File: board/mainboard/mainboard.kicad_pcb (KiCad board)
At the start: 2 copper layers, 148.1 x 58.4 mm, 97 parts, among them J1 BACKL, P1 I2C, P10 BUMPERS, P12 POWER, P2 Motor1, P3 Motor2, P4 SPI, P5 DAC, P6 LINE SENSORS, P7 ANALOG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

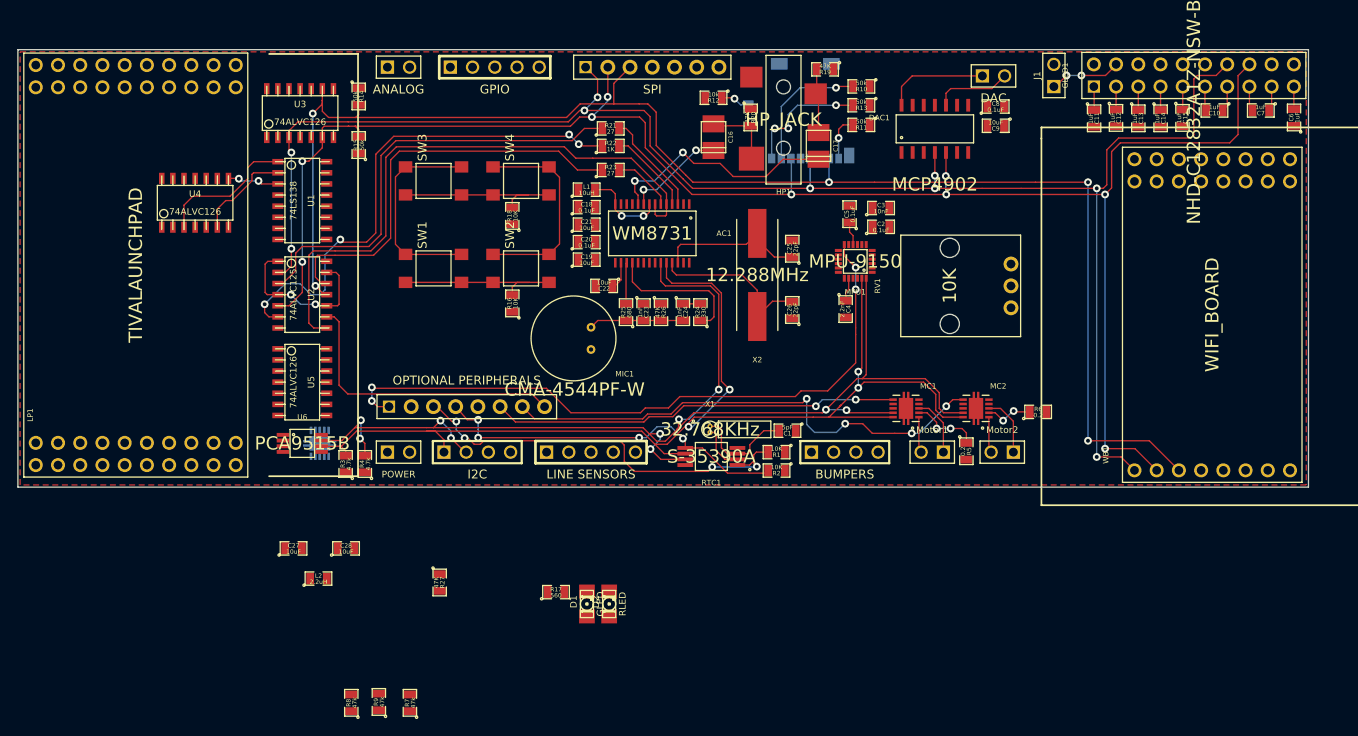
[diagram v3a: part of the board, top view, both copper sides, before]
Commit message: All but Spi_CS and power are routed.
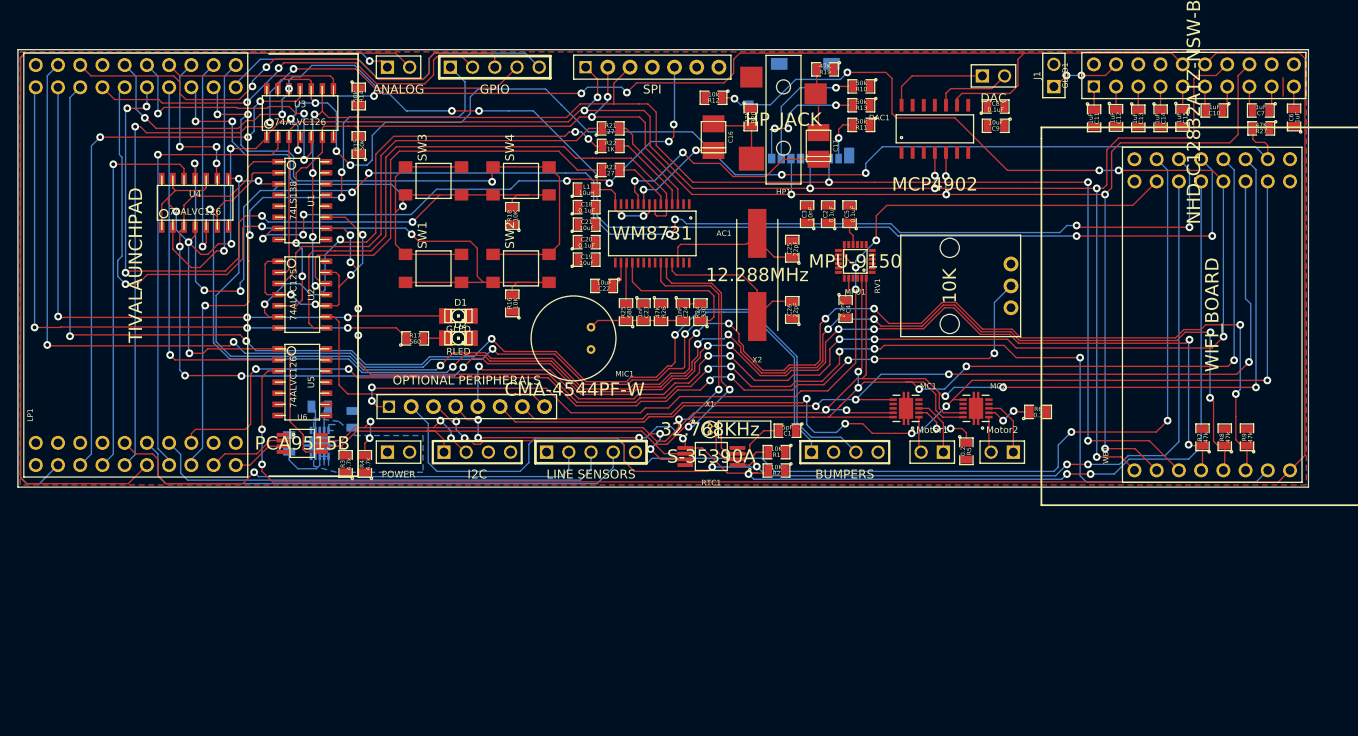
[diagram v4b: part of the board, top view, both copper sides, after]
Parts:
- C27, C28, L2: moved to B.Cu
- moved R27 107.3 mm to (269.6, 119.0), turned to 180 degrees
- moved R8 104.3 mm to (265.4, 154.3)
- moved R9 103.7 mm to (268.0, 154.3)
- moved R7 95.5 mm to (262.9, 154.3)
- moved D1 36.1 mm to (177.8, 140.4), turned to 0 degrees
- moved D2 34.9 mm to (177.8, 143.0), turned to 0 degrees
- moved R17 33.2 mm to (172.9, 143.0)
- moved L2 19.7 mm to (162.0, 150.8), turned to 180 degrees
- moved C28 14.8 mm to (165.8, 152.2), turned to 90 degrees
- moved C27 12.0 mm to (158.5, 155.0), turned to 90 degrees
- moved C3 8.48 mm to (217.7, 128.8), turned to 90 degrees
- moved C2 6.22 mm to (220.1, 128.8), turned to 90 degrees
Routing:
- net CC_CONTROL: track 0.00 -> 232.1 mm, vias 0 -> 12
- net GLCD_A0: track 0.00 -> 191.4 mm, vias 0 -> 2
- net SD_SWITCH: track 3.36 -> 183.4 mm, vias 1 -> 10
- net SPI_SEL2: track 5.91 -> 181.8 mm, vias 2 -> 9
- net SPI_SEL1: track 11.2 -> 176.6 mm, vias 0 -> 8
- net SPI_SEL0: track 16.0 -> 178.4 mm, vias 0 -> 10
- net UART_TX: track 0.00 -> 157.7 mm, vias 0 -> 9
- net RST: track 0.00 -> 145.0 mm, vias 0 -> 5
- net SPI_CS5: track 0.00 -> 144.1 mm, vias 0 -> 9
- net BUMP1: track 0.00 -> 141.2 mm, vias 0 -> 4
- net BUMP2: track 0.00 -> 140.0 mm, vias 0 -> 4
- net WIFI_INT: track 0.00 -> 132.4 mm, vias 0 -> 2
- net UART_RX: track 0.00 -> 127.3 mm, vias 0 -> 5
- net POT: track 0.00 -> 113.2 mm, vias 0 -> 7
- net AIN2: track 0.00 -> 108.9 mm
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- added copper zone on B.Cu, net N-00000121

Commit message: All finished but the power and GND
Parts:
- moved R15 0.78 mm to (165.7, 120.7)
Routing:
- net SPI_CS3: track 0.00 -> 129.3 mm, vias 0 -> 3
- net SPI_CS2: track 0.00 -> 96.1 mm, vias 0 -> 4
- net SPI_CS6: track 0.00 -> 57.9 mm, vias 0 -> 6
- net UART_RX: track 127.3 -> 131.4 mm
- net (no net): track 2.10 -> 0.00 mm
- net KPAD_C1: track 93.1 -> 95.1 mm
- net SPI_CS5: track 144.1 -> 145.8 mm
- net SD_SWITCH: track 183.4 -> 185.0 mm
- net UART_TX: track 157.7 -> 159.3 mm
- net SPI_MOSI: track 202.0 -> 203.5 mm
- net SPI_SCK: track 192.4 -> 193.8 mm
- net KPAD_C2: track 85.3 -> 86.6 mm
- net SPI_MISO: track 171.5 -> 172.8 mm
- net SPI_CS7: track 63.7 -> 64.6 mm
- net PA5: track 74.4 -> 75.2 mm

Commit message: Finished Rev1.1, everything is connected, but not double checked yet
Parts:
- moved R15 0.80 mm to (166.5, 120.7)
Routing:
- net GND: track 0.00 -> 426.7 mm, vias 0 -> 28
- net 3V3: track 0.00 -> 377.7 mm, vias 0 -> 48
- net SPI_CS1: track 15.1 -> 97.4 mm, vias 1 -> 5
- net (no net): track 0.00 -> 5.40 mm, vias 0 -> 2
- net SPI_CS3: track 129.3 -> 134.4 mm
- net RST: track 145.0 -> 149.0 mm
- net CC_CONTROL: track 232.1 -> 235.8 mm, vias 12 -> 14
- net PA5: track 75.2 -> 72.2 mm
- net BUMP1: track 141.2 -> 138.5 mm, vias 4 -> 6
- net MPUINT: track 117.3 -> 119.7 mm
- net KPAD_C2: track 86.6 -> 89.1 mm, vias 5 -> 9
- net SPI_CS6: track 57.9 -> 55.6 mm, vias 6 -> 5
- net BUMP2: track 140.0 -> 138.1 mm, vias 4 -> 6
- net SPI_MISO_LP: track 20.5 -> 22.0 mm
- net SPI_CS7: track 64.6 -> 65.9 mm
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- added copper zone on B.Cu, net 3V3
- added copper zone on B.Cu, net GND

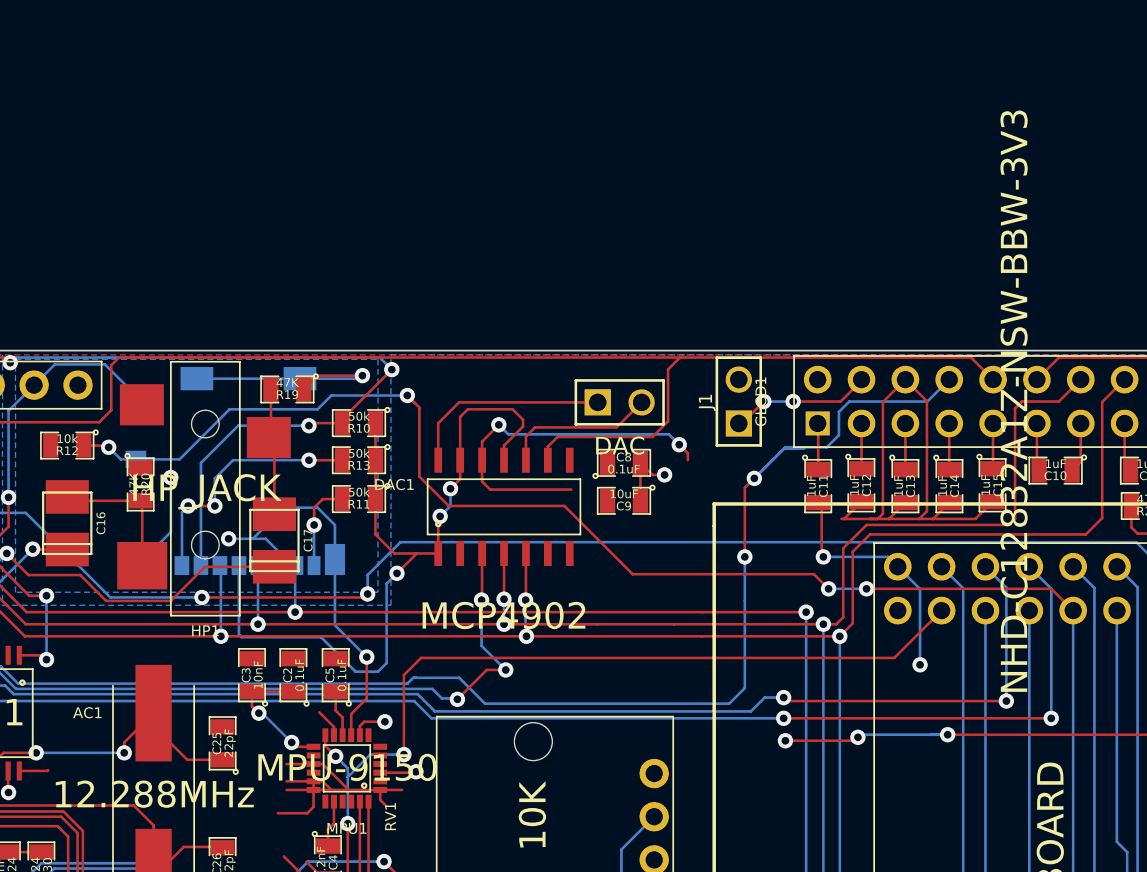
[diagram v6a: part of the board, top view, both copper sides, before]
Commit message: Removed traces from holes
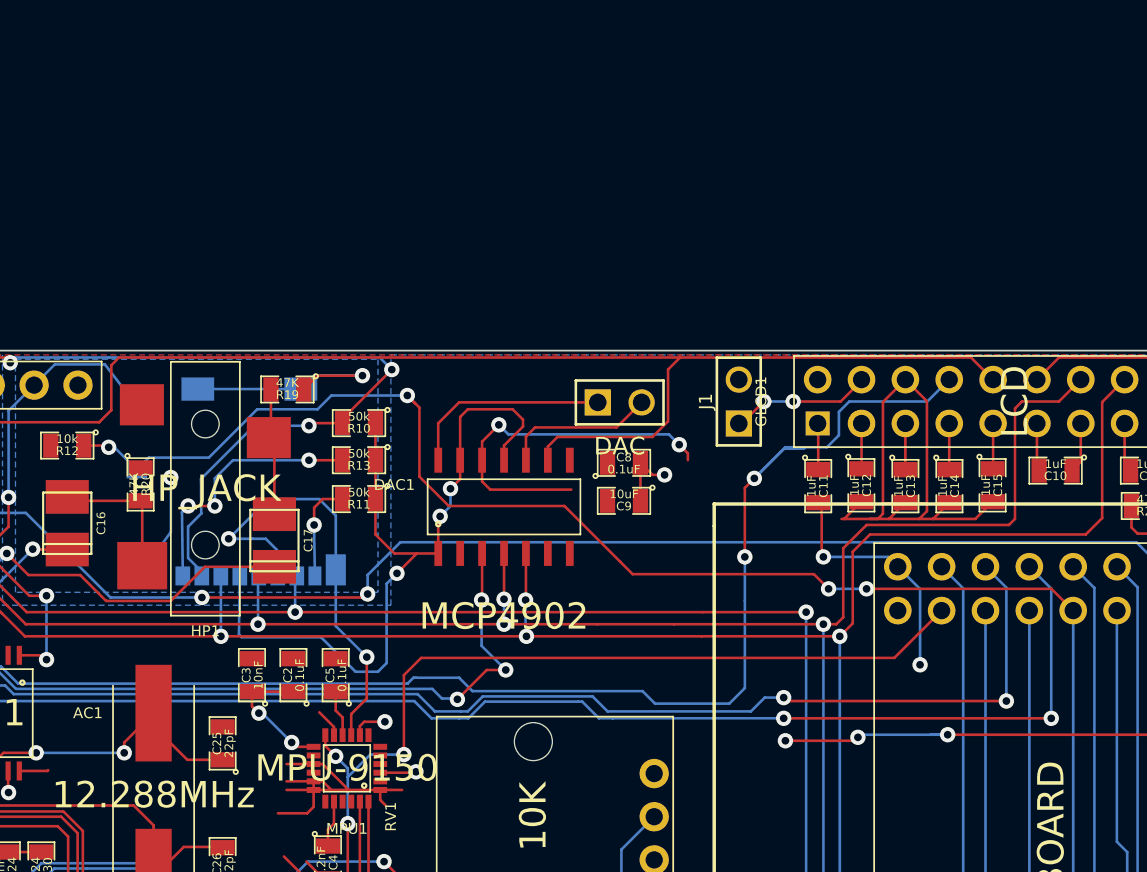
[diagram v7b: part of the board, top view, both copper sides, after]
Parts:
- GLCD1: value NHD-C12832A1Z-NSW-BBW-3V3 -> LCD
- moved SD1 0.60 mm to (216.8, 117.6)
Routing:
- net GND: track 426.7 -> 430.1 mm
- net UART_RX: track 132.0 -> 132.8 mm
- net UART_TX: track 160.5 -> 161.2 mm
- net SPI_CS1: track 97.4 -> 98.1 mm
- net SPI_MOSI: track 203.5 -> 202.9 mm
- net N-0000050: track 5.21 -> 5.81 mm
- net N-0000049: track 14.6 -> 15.2 mm
- net SPI_SCK: track 194.3 -> 193.7 mm
- net SPI_MISO: track 172.8 -> 172.2 mm

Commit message: Cleaning up busses
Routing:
- net I2C_CL: track 199.6 -> 201.5 mm
- net I2C_DA: track 209.6 -> 211.0 mm
- net MOTOR2F: track 117.1 -> 118.3 mm, vias 3 -> 5
- net MOTOR1F: track 114.9 -> 116.0 mm, vias 4 -> 6
- net MPUINT: track 119.7 -> 120.6 mm, vias 5 -> 7
- net BUMP1: track 138.5 -> 137.6 mm
- net SPI_SEL2: track 181.6 -> 181.1 mm
- net SPI_SEL1: track 176.5 -> 177.0 mm
